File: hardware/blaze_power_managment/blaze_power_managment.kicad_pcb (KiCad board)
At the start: 2 copper layers, 70 x 70 mm, 2 parts, among them J2 Conn_01x30_Pin, J3 Conn_01x30_Socket

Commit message: Component assingment
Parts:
- added C1: 4.7nF, Capacitor_SMD:C_0603_1608Metric, F.Cu at (152.5, 127.8)
- added C10: 470nF, Capacitor_SMD:C_0603_1608Metric, F.Cu at (198.3, 113.0)
- added C11: 0.1uF, Capacitor_SMD:C_0603_1608Metric, F.Cu at (198.3, 115.5)
- added C12: 6.8uF, Capacitor_SMD:C_0603_1608Metric, F.Cu at (198.3, 118.0)
- added C13: 6.8uF, Capacitor_SMD:C_0603_1608Metric, F.Cu at (202.3, 98.0)
- added C14: 2.2nF, Capacitor_SMD:C_0603_1608Metric, F.Cu at (202.3, 100.5)
- added C15: 22uF, Capacitor_SMD:C_0603_1608Metric, F.Cu at (202.3, 103.0)
- added C16: 22uF, Capacitor_SMD:C_0603_1608Metric, F.Cu at (202.3, 105.5)
- added C17: 22uF, Capacitor_SMD:C_0603_1608Metric, F.Cu at (202.3, 108.0)
- added C18: 470nF, Capacitor_SMD:C_0603_1608Metric, F.Cu at (202.3, 110.5)
- added C19: 2.2uF, Capacitor_SMD:C_0603_1608Metric, F.Cu at (200.9, 137.0)
- added C2: 0.1uF, Capacitor_SMD:C_0603_1608Metric, F.Cu at (147.7, 136.0)
- added C20: 0.1uF, Capacitor_SMD:C_0603_1608Metric, F.Cu at (200.9, 139.5)
- added C21: 4.7uF, Capacitor_SMD:C_0603_1608Metric, F.Cu at (200.9, 142.1)
- added C22: 0.1uF, Capacitor_SMD:C_0603_1608Metric, F.Cu at (201.2, 144.5)
- added C23: 1uF, Capacitor_SMD:C_0603_1608Metric, F.Cu at (201.2, 147.0)
- added C24: 0.1uF, Capacitor_SMD:C_0603_1608Metric, F.Cu at (201.2, 149.5)
- added C25: 0.1uF, Capacitor_SMD:C_0603_1608Metric, F.Cu at (222.7, 132.5)
- added C26: 2.2uF, Capacitor_SMD:C_0603_1608Metric, F.Cu at (206.4, 108.0)
- added C3: 0.1uF, Capacitor_SMD:C_0603_1608Metric, F.Cu at (151.2, 131.5)
- added C4: 6.8uF, Capacitor_SMD:C_0603_1608Metric, F.Cu at (198.3, 98.0)
- added C5: 6.8uF, Capacitor_SMD:C_0603_1608Metric, F.Cu at (198.3, 100.5)
- added C6: 2.2nF, Capacitor_SMD:C_0603_1608Metric, F.Cu at (198.3, 103.0)
- added C7: 22uF, Capacitor_SMD:C_0603_1608Metric, F.Cu at (198.3, 105.5)
- added C8: 22uF, Capacitor_SMD:C_0603_1608Metric, F.Cu at (198.3, 108.0)
- added C9: 22uF, Capacitor_SMD:C_0603_1608Metric, F.Cu at (198.3, 110.5)
- added D1: ESDCAN03-2BM3Y, Package_TO_SOT_SMD:SOT-416, F.Cu at (147.8, 125.9)
- added D2: D_Zener, Diode_SMD:D_0603_1608Metric, F.Cu at (145.2, 88.1)
- added D3: LED, LED_SMD:LED_0603_1608Metric, F.Cu at (214.4, 105.0)
- added D4: LED, LED_SMD:LED_0603_1608Metric, F.Cu at (214.4, 107.6)
- added D5: D_Schottky, Diode_SMD:D_0603_1608Metric, F.Cu at (222.8, 130.5)
- added F1: Polyfuse, Fuse:Fuse_1206_3216Metric, F.Cu at (147.5, 88.0)
- added FL1: Choke, Inductor_SMD:L_CommonModeChoke_Coilcraft_0603USB, F.Cu at (147.8, 128.5)
- added J3: XT30, Connector_AMASS:AMASS_XT30PW-M_1x02_P2.50mm_Horizontal, F.Cu at (135.5, 89.2)
- added J4: XT30, Connector_AMASS:AMASS_XT30PW-M_1x02_P2.50mm_Horizontal, F.Cu at (127.8, 103.2)
- added J5: JTAG, Connector_PinHeader_1.00mm:PinHeader_2x05_P1.00mm_Vertical_SMD, F.Cu at (224.2, 147.0)
- added L1: 4.6uH 12.1mOhm, Inductor_SMD:L_SXN_SMDRI124, F.Cu at (225.3, 103.3)
- added L2: 4.6uH 12.1mOhm, Inductor_SMD:L_SXN_SMDRI124, F.Cu at (225.3, 117.2)
- added Q1: DMG2305, Package_TO_SOT_SMD:SOT-23-3, F.Cu at (142.2, 88.0)
- added R1: 60, Resistor_SMD:R_0603_1608Metric, F.Cu at (150.0, 127.8)
- added R10: 0.02, Resistor_SMD:R_0603_1608Metric, F.Cu at (210.4, 103.0)
- added R11: 15k, Resistor_SMD:R_0603_1608Metric, F.Cu at (210.4, 105.5)
- added R12: 10k, Resistor_SMD:R_0603_1608Metric, F.Cu at (210.4, 108.0)
- added R13: 80, Resistor_SMD:R_0603_1608Metric, F.Cu at (210.4, 110.5)
- added R14: 4.75k, Resistor_SMD:R_0603_1608Metric, F.Cu at (210.4, 113.0)
- added R2: 60, Resistor_SMD:R_0603_1608Metric, F.Cu at (145.5, 127.8)
- added R3: 10K, Resistor_SMD:R_0603_1608Metric, F.Cu at (144.5, 131.6)
- added R4: 0.02, Resistor_SMD:R_0603_1608Metric, F.Cu at (206.4, 110.5)
- added R5: 25.5k, Resistor_SMD:R_0603_1608Metric, F.Cu at (206.4, 113.0)
- added R6: 10k, Resistor_SMD:R_0603_1608Metric, F.Cu at (206.4, 115.5)
- added R7: 165, Resistor_SMD:R_0603_1608Metric, F.Cu at (206.4, 118.0)
- added R8: R_US, Resistor_SMD:R_0603_1608Metric, F.Cu at (142.2, 91.4)
- added R9: 4.75k, Resistor_SMD:R_0603_1608Metric, F.Cu at (210.4, 100.5)
- added SW1: SW_SPST, Button_Switch_SMD:SW_SPST_B3U-1000P, F.Cu at (222.3, 137.0)
- added SW2: SW_SPDT, Button_Switch_SMD:Nidec_Copal_CAS-120A, F.Cu at (206.3, 138.0)
- added U1: TCAN1044VDDFR, Package_SON:Texas_S-PVSON-N8, F.Cu at (147.7, 132.2)
- added U2: TPS62913, Blaze_Library:TPS62913R, F.Cu at (235.1, 101.4)
- added U3: INA2181, Blaze_Library:WSON10-DSQ0010A_TEX, F.Cu at (239.1, 109.1)
- added U4: TPS62913, Blaze_Library:TPS62913R, F.Cu at (235.1, 105.7)
- added U5: STM32H503KBUx, Package_DFN_QFN:QFN-32-1EP_5x5mm_P0.5mm_EP3.45x3.45mm, F.Cu at (214.8, 139.1)
- renumbered J2 to J1, J3 to J2
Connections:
- net /RX_RADIO renamed Net-(J1-Pin_6)
- net /TX_RADIO renamed Net-(J1-Pin_5)
- J1 pad 1: Net-(J2-Pin_1) -> VBATT
- J1 pad 2: Net-(J2-Pin_2) -> VBATT
- J2 pad 29: Net-(J2-Pin_2) -> VBATT
- J2 pad 30: Net-(J2-Pin_1) -> VBATT
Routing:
- net +5V: track 0.00 -> 33.1 mm, vias 0 -> 7
- net GND: track 0.00 -> 18.2 mm, vias 0 -> 10
- net +3V3: track 0.00 -> 12.4 mm, vias 0 -> 6
- net /CANH: track 0.00 -> 8.34 mm, vias 0 -> 2
- net Net-(C1-Pad1): track 0.00 -> 7.28 mm
- net /CANL: track 0.00 -> 6.90 mm, vias 0 -> 1
- net VBATT: track 0.00 -> 4.53 mm, vias 0 -> 2
- net /PPS: track 0.00 -> 2.33 mm, vias 0 -> 1
- net Net-(J1-Pin_10): track 0.00 -> 2.30 mm, vias 0 -> 1
- net /CAN_STB: track 0.00 -> 2.27 mm
- net Net-(J1-Pin_19): track 0.00 -> 2.26 mm, vias 0 -> 1
- net Net-(J1-Pin_20): track 0.00 -> 2.26 mm, vias 0 -> 1
- net Net-(J1-Pin_16): track 0.00 -> 2.23 mm, vias 0 -> 1
- net Net-(J1-Pin_17): track 0.00 -> 2.18 mm, vias 0 -> 1
- net Net-(J1-Pin_5): track 0.00 -> 2.16 mm, vias 0 -> 1
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- added copper zone on In1.Cu, net +3V3
- added copper zone on In2.Cu, net GND
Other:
- copper layers 2 -> 4

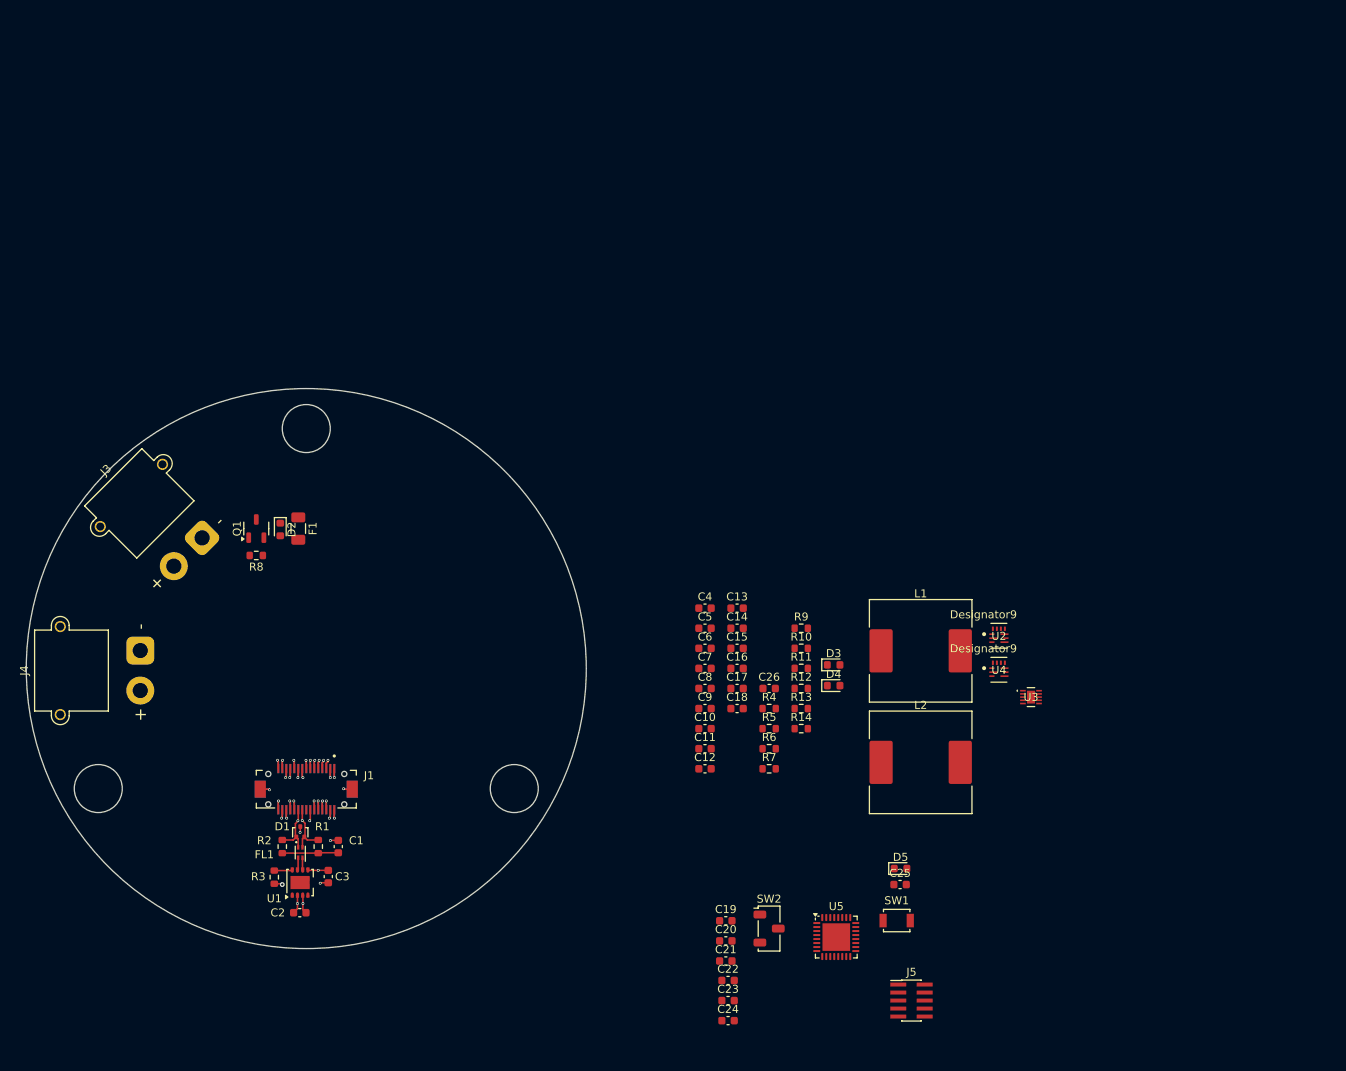
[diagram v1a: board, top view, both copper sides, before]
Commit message: Component grouping
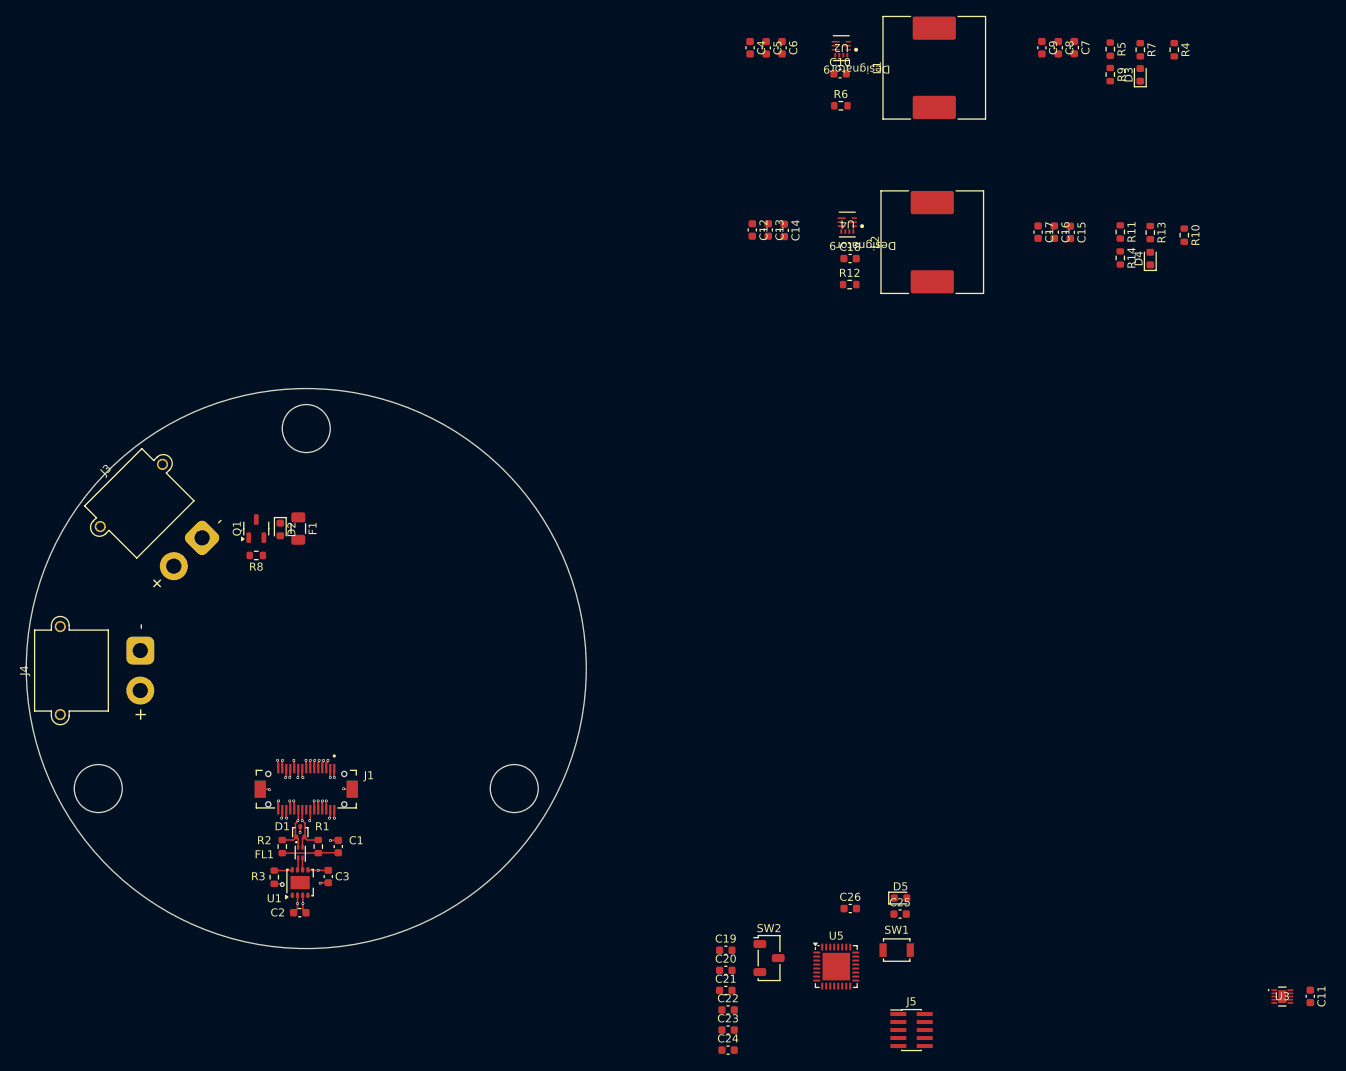
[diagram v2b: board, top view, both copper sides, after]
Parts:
- moved R7 101.1 mm to (252.8, 28.1), turned to -90 degrees
- moved R4 96.7 mm to (257.0, 28.1), turned to -90 degrees
- moved R5 95.0 mm to (249.0, 28.1), turned to -90 degrees
- moved C9 92.7 mm to (240.4, 27.9), turned to -90 degrees
- moved C8 91.5 mm to (242.5, 27.9), turned to -90 degrees
- moved C7 90.3 mm to (244.5, 27.9), turned to -90 degrees
- moved C10 83.6 mm to (215.2, 31.1)
- moved D3 83.1 mm to (252.8, 31.3), turned to 90 degrees
- moved C11 81.7 mm to (274.0, 146.5), turned to -90 degrees
- moved R6 80.9 mm to (215.3, 35.1)
- moved R9 79.3 mm to (249.0, 31.2), turned to -90 degrees
- moved U2 76.1 mm to (215.4, 27.9), turned to 180 degrees
- moved C6 75.7 mm to (208.0, 27.9), turned to -90 degrees
- moved R13 73.8 mm to (254.0, 51.0), turned to -90 degrees
- moved C5 73.0 mm to (206.0, 27.9), turned to -90 degrees
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
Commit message: Power layout
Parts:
- moved D3 125.1 mm to (142.0, 89.5)
- moved R7 125.1 mm to (142.0, 86.3)
- moved D4 124.5 mm to (141.8, 108.0)
- moved R13 124.5 mm to (141.8, 104.8)
- moved R5 120.0 mm to (144.0, 86.2)
- moved R9 120.0 mm to (144.0, 89.4)
- moved R11 119.3 mm to (143.8, 104.8)
- moved R14 119.3 mm to (143.8, 108.0)
- moved C7 115.0 mm to (147.0, 88.8), turned to 180 degrees
- moved R4 114.3 mm to (155.4, 80.5), turned to 180 degrees
- moved R10 113.7 mm to (155.0, 99.0), turned to 180 degrees
- moved C15 112.6 mm to (146.5, 107.3), turned to 180 degrees
- moved C8 112.2 mm to (146.9, 86.8), turned to 180 degrees
- moved C16 109.8 mm to (146.6, 105.3), turned to 180 degrees
- moved C9 109.4 mm to (146.9, 84.7), turned to 180 degrees
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
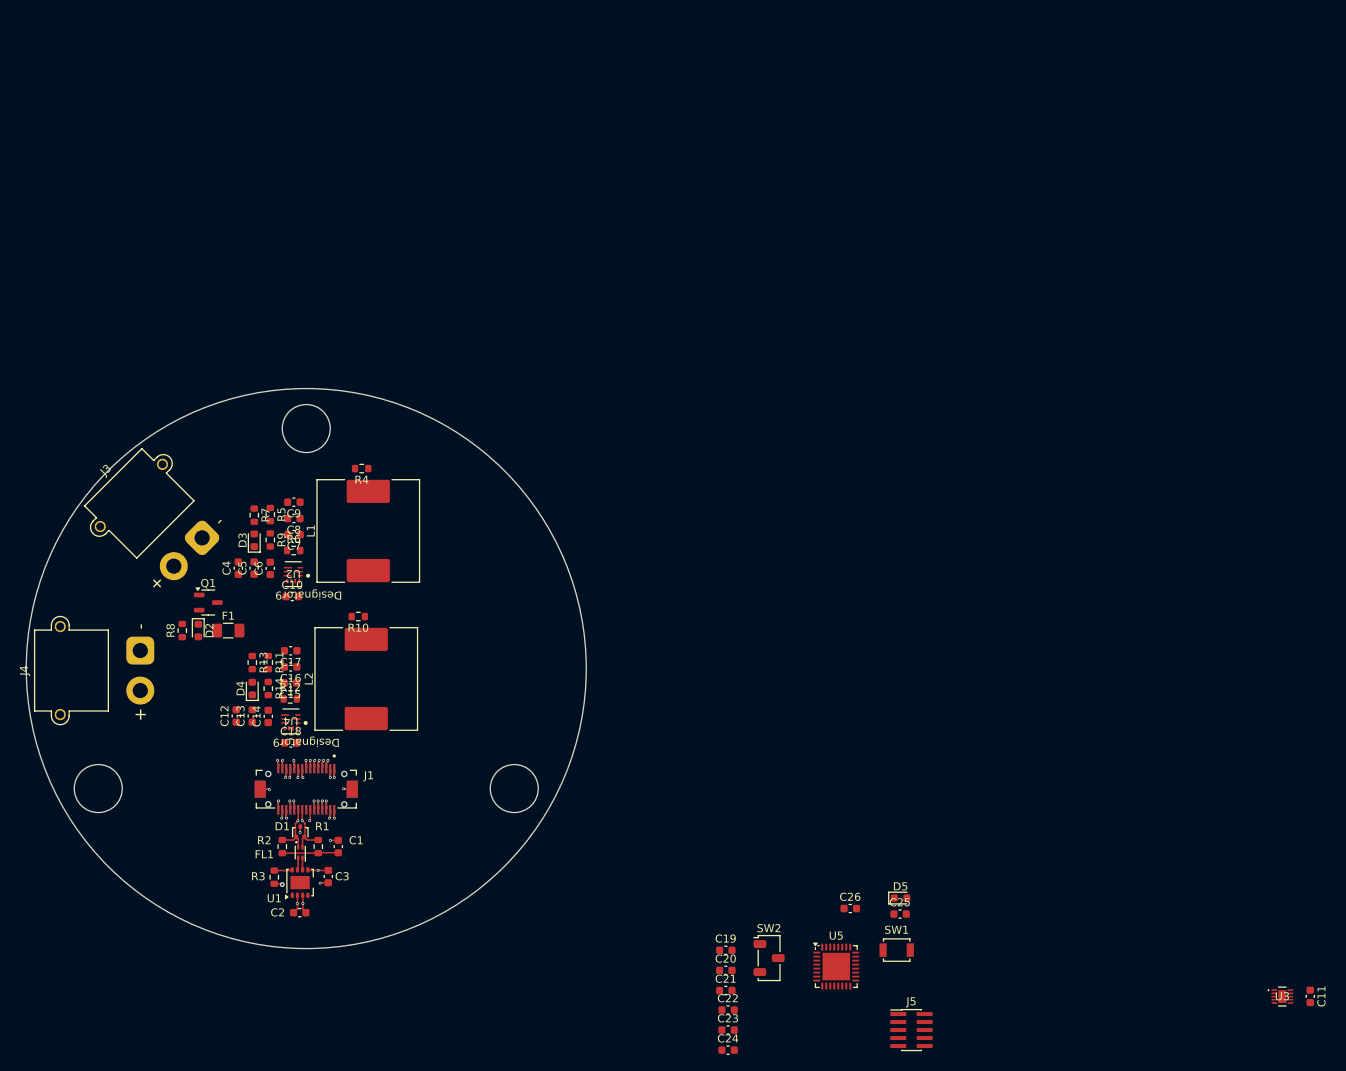
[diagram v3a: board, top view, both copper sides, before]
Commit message: Component layout draft
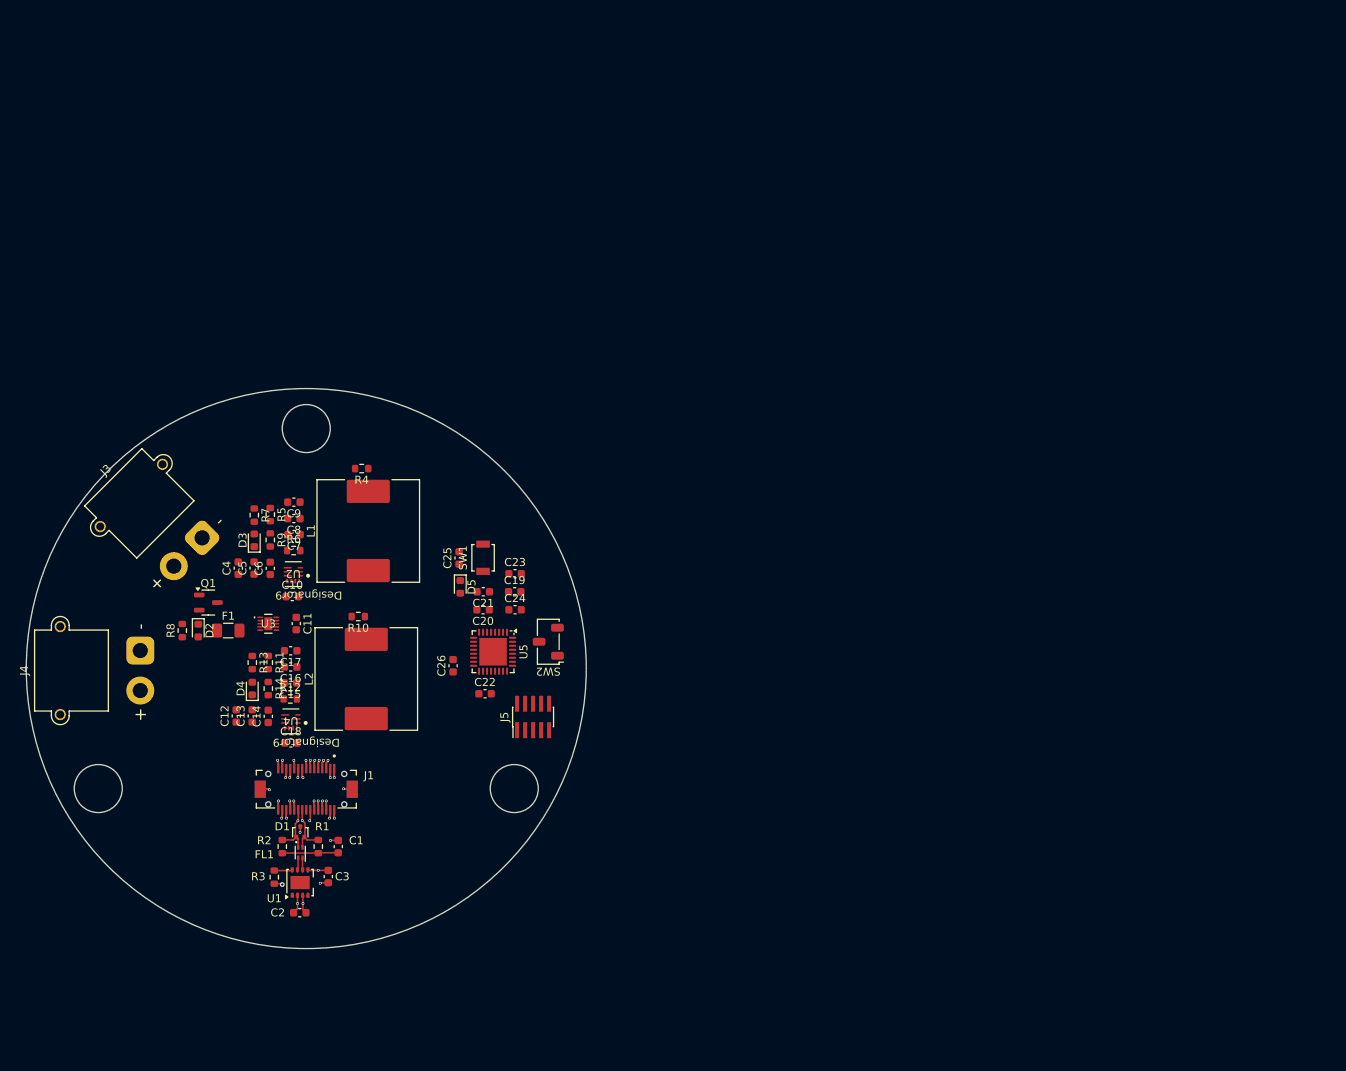
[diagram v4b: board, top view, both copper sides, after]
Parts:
- moved U3 135.0 mm to (143.8, 99.9)
- moved C11 135.0 mm to (147.2, 99.9)
- moved SW1 71.3 mm to (170.6, 91.7), turned to 90 degrees
- moved C25 70.9 mm to (167.6, 91.7), turned to 90 degrees
- moved D5 67.4 mm to (167.8, 95.3), turned to -90 degrees
- moved C23 62.9 mm to (174.6, 93.7)
- moved J5 61.4 mm to (176.8, 111.5), turned to 90 degrees
- moved C24 61.1 mm to (174.6, 98.2)
- moved C21 58.3 mm to (170.6, 95.9), turned to 180 degrees
- moved U5 58.2 mm to (171.8, 103.4), turned to -90 degrees
- moved C26 58.2 mm to (166.8, 105.2), turned to 90 degrees
- moved C20 54.3 mm to (170.6, 98.2), turned to 180 degrees
- moved C19 52.0 mm to (174.6, 95.9)
- moved C22 49.9 mm to (170.8, 108.7)
- moved SW2 48.2 mm to (178.8, 102.2), turned to 180 degrees
